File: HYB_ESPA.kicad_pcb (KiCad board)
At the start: 2 copper layers, 100 x 60 mm, 146 parts, among them J10 Y_J1, J11 X_J1, J12 Y_J2, J13 Y_Stepper, J14 X_J2, J15 AnIn, J16 AirSW, J17 PWM2_Drive, J18 PWM2_Drive, J19 5V FAN, J2 USB_C, J20 Micro_SD_Card_Det1, J21 PowerIn, J22 AirOut, J23 EmStop, J24 Z_LIM1, J25 Z_LIM2, J26 Y_LIM1, J27 X_LIM1, J28 Y_LIM2, J29 X_LIM2, J3 E_Stepper, J30 Probe, J31 UART, J4 E_J2, J5 E_J1, J6 Z_Stepper, J7 Z_J1, J8 Z_J2, J9 X_Stepper, Q1 IRF4905, Q10 PJA3440, Q2 PJA3440, Q3 IRF4905, Q4 PJA3440, Q5 PJA3440, Q6 PJA3440, Q7 PJA3440, Q8 PJA3440, Q9 PJA3440, SW1 SW_Reset, U1 SMF05CT1G, U10 AP63201, U11 SN74LVC1T45DBV, U2 CH340E, U3 Stepper Breakout, U4 Stepper Breakout, U5 Stepper Breakout, U6 Stepper Breakout, U7 ESP32, U8 AP7366, U9 SN74LVC1T45DBV

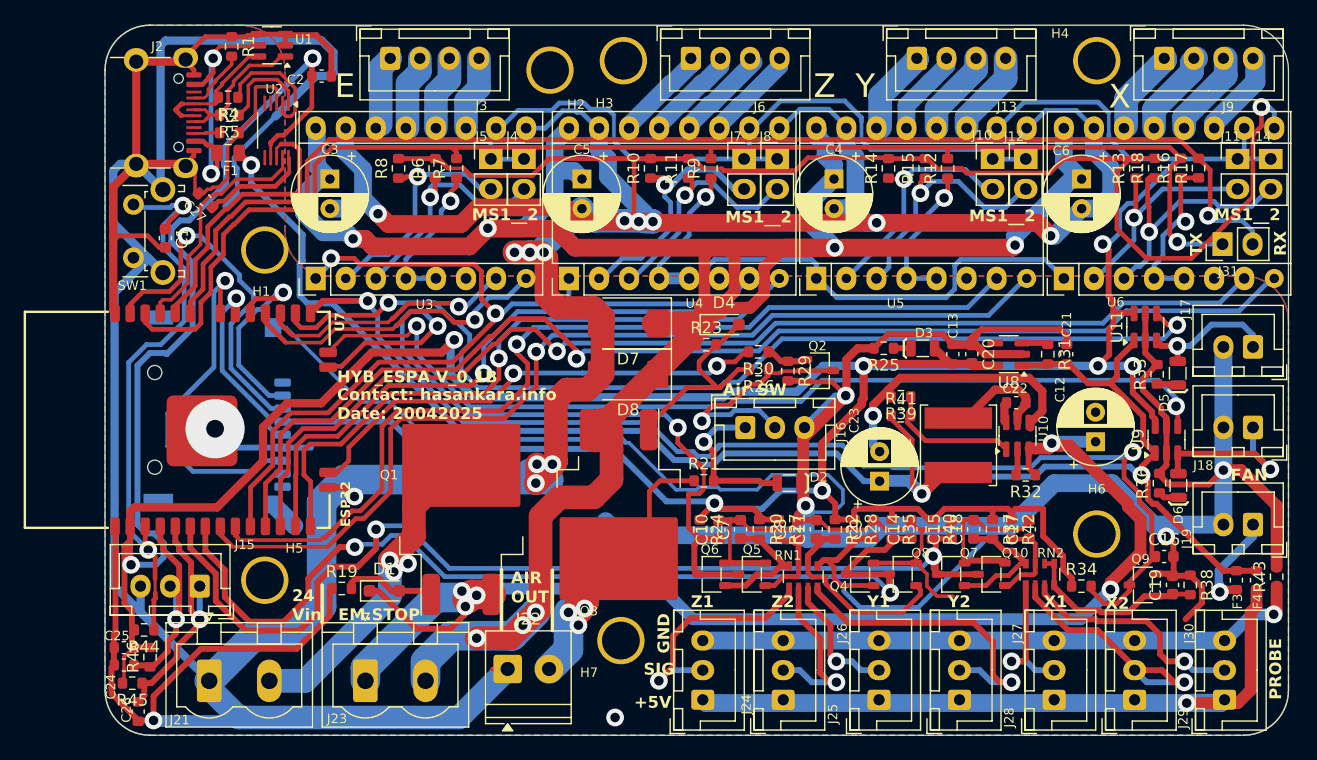
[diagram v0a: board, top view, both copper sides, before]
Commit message: Fixed component name positions in, Top silk, F. Fab, and ibom, files.
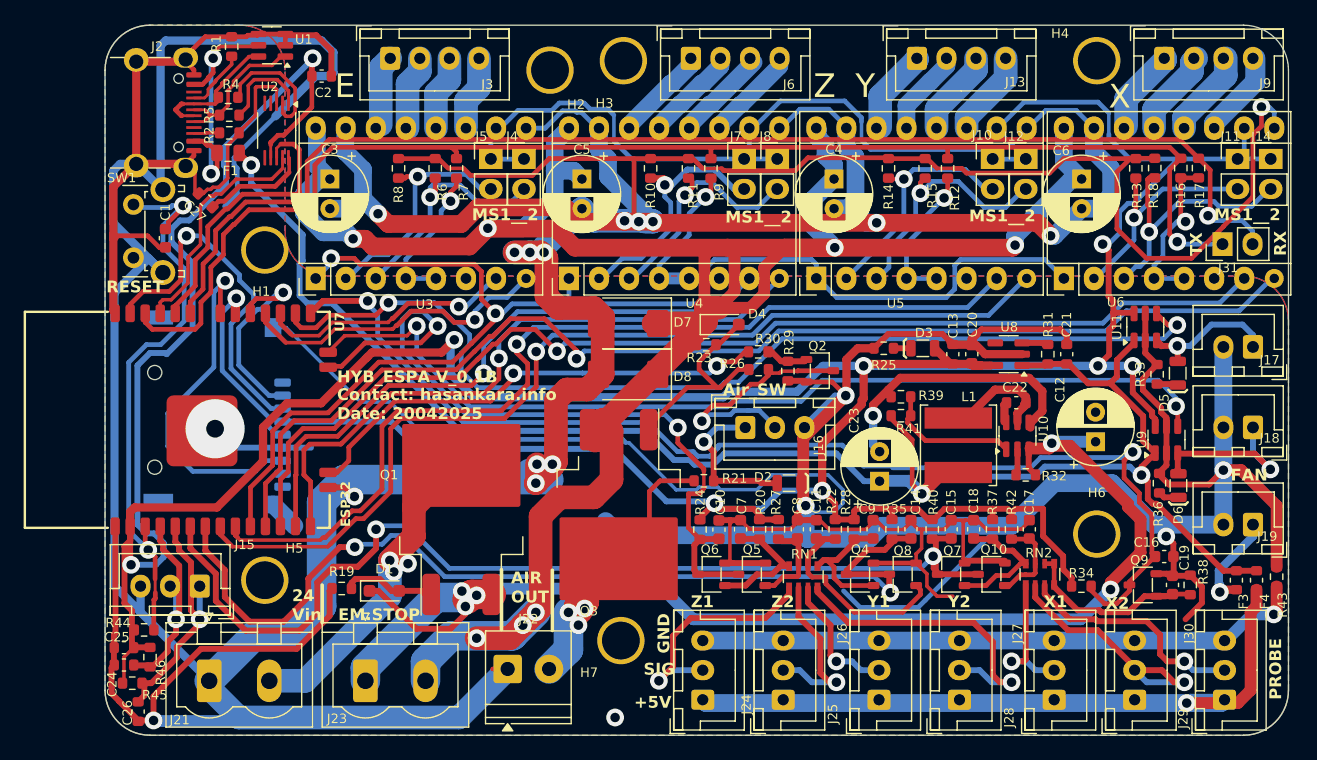
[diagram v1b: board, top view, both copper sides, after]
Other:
- board text added: "RESET"
